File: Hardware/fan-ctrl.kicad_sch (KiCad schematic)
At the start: 52 parts, among them CN1 DB127S-3.5-4P-GN, Q1 AO3401A, Q2 AO3400A, U1 STM32G070RBT6, U2 826629-3, U3 826629-3, U4 MP2359DT-LF-Z, U5 XDJK-0051-025, U6 AMS1117-3.3, Y1 Crystal_GND24

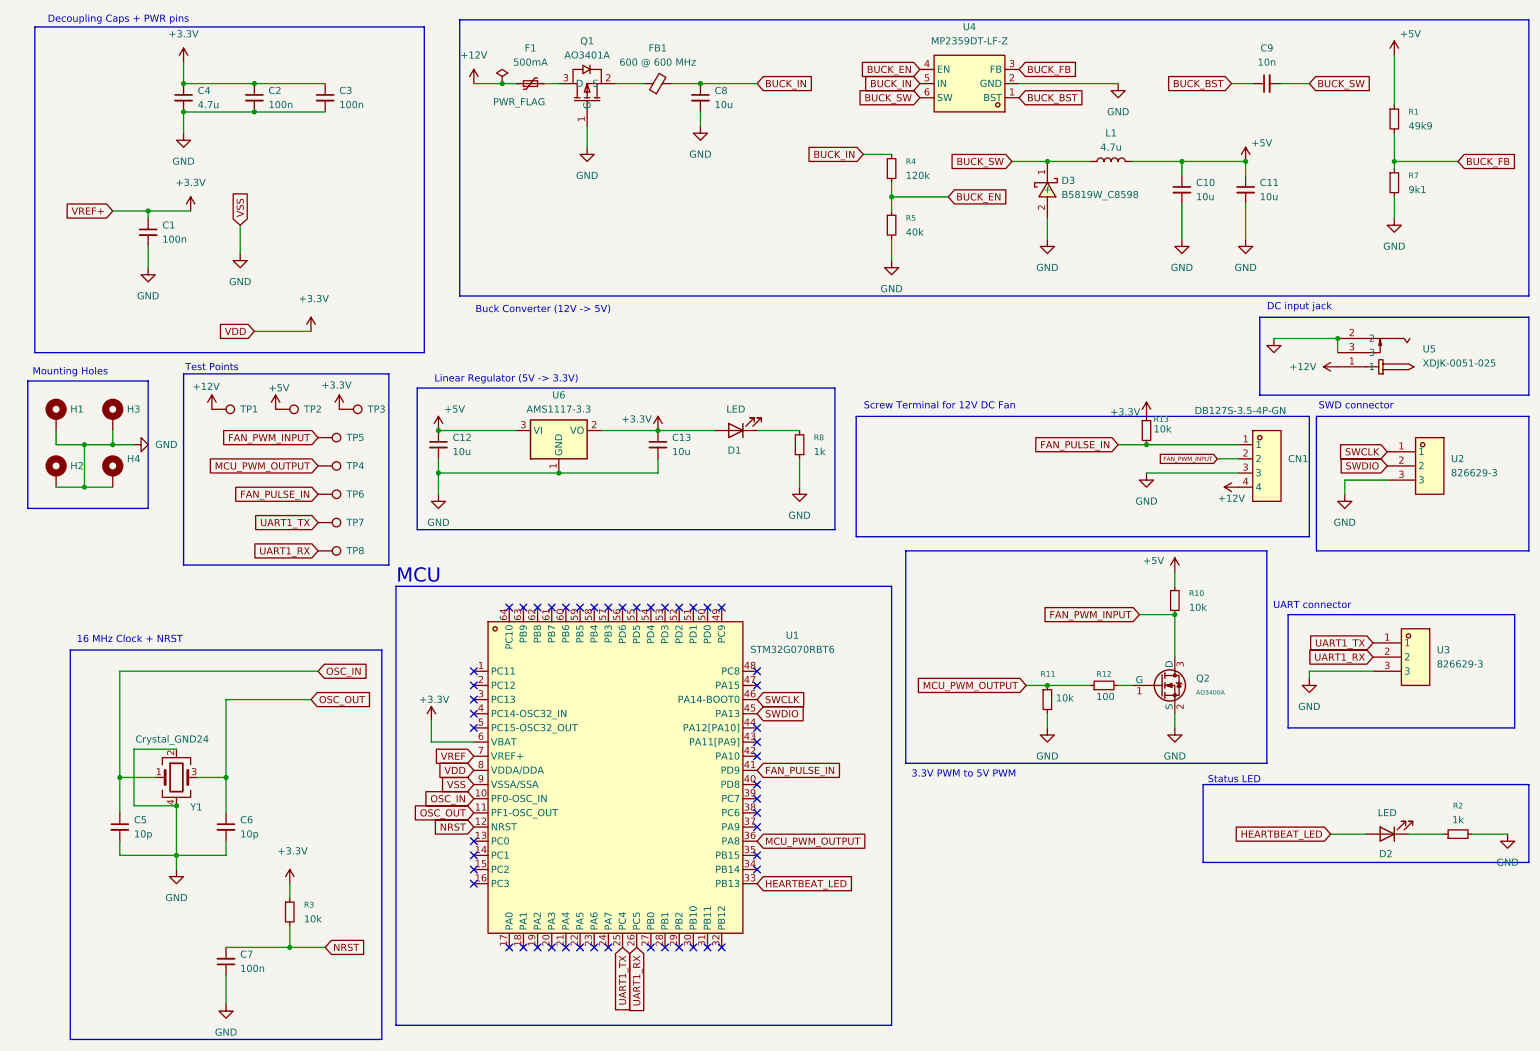
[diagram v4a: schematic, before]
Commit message: Update schematics (polyfuse value, capacitor values in linear regulatorcircuit, use different HW timer enabled pin for the fan pulse input
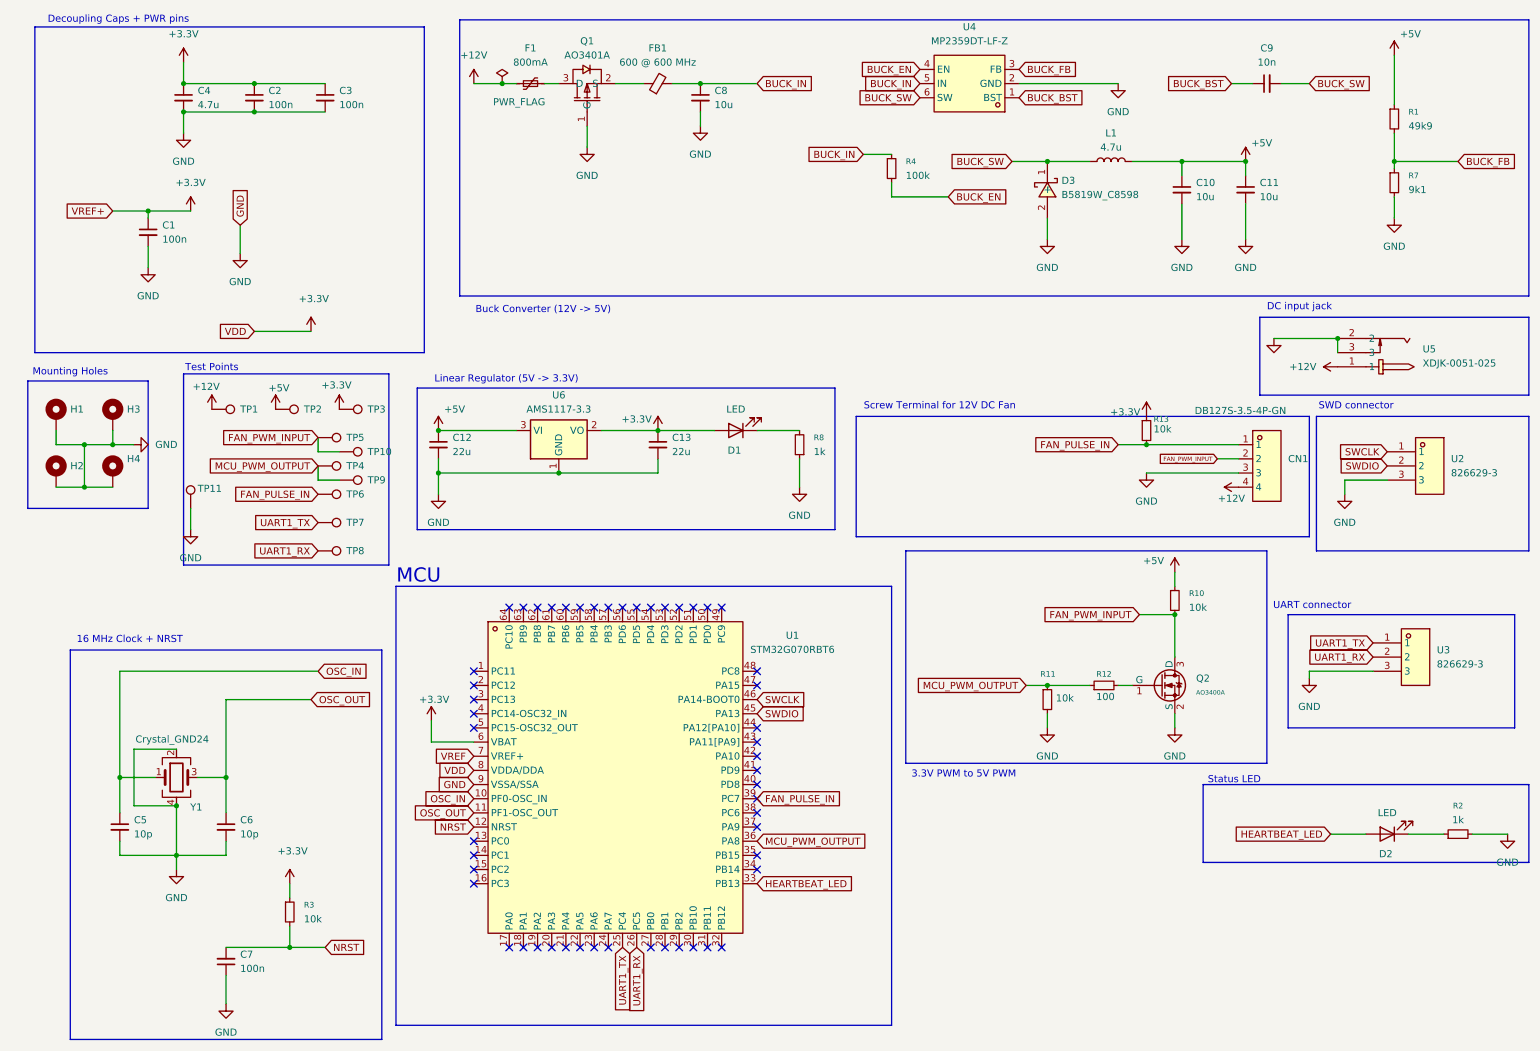
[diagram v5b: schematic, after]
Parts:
- removed R5: 40k, PCM_JLCPCB:R_0603, symbol Device:R_Small
- added TP10, TP11, TP9: TestPoint, TestPoint:TestPoint_THTPad_D1.0mm_Drill0.5mm, symbol Connector:TestPoint
- C12, C13: value 10u -> 22u
- F1: value 500mA -> 800mA
- R4: value 120k -> 100k
- TP1, TP2, TP3, TP5, TP6: footprint TestPoint:TestPoint_Pad_D2.5mm -> TestPoint:TestPoint_Pad_D3.0mm
- TP4: footprint TestPoint:TestPoint_Pad_D1.0mm -> TestPoint:TestPoint_Pad_D2.0mm
- TP7, TP8: footprint TestPoint:TestPoint_Pad_D1.5mm -> TestPoint:TestPoint_Pad_D2.0mm
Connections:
- net FAN_PULSE_IN: now also U1.39 (PC7); no longer U1.41 (PD9)
- net FAN_PWM_INPUT: now also TP10.1
- net GND: now also TP11.1
- net MCU_PWM_OUTPUT: now also TP9.1
- no-connect marks 50 -> 51
